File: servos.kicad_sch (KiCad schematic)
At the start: 14 parts, among them J10 Conn_01x03, J11 Conn_01x03, J6 Conn_01x03, J7 Conn_01x03, J8 Conn_01x03, J9 Conn_01x03, U10 INA745A, U11 INA745A, U12 INA745A, U13 INA745A, U15 SN74LVC8T245, U6 INA745A, U9 INA745A

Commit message: got it to fit in about the right shape
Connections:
- net +3V3: now also U15.1 (V_{CCA})
- net GND: now also U15.11 (GND), U15.12 (GND), U15.13 (GND)
- net +5V: now reaches U15.23 (V_{CCB}), U15.24 (V_{CCB})
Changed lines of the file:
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@@
+	)
+	(symbol
+		(lib_id "power:+3V3")
+		(at 341.63 46.99 0)
+		(unit 1)
+		(exclude_from_sim no)
+		(in_bom yes)
+		(on_board yes)
+		(dnp no)
+		(fields_autoplaced yes)
+		(property "Reference" "#PWR081"
+			(at 341.63 50.8 0)
+			(effects
+				(font
+					(size 1.27 1.27)
+				)
+				(hide yes)
+			)
+		)
+		(property "Value" "+3V3"
+			(at 341.63 41.91 0)
+			(effects
+				(font
+					(size 1.27 1.27)
+				)
+			)
+		)
+		(property "Footprint" ""
+			(at 341.63 46.99 0)
+			(effects
+				(font
+					(size 1.27 1.27)
+				)
+				(hide yes)
+			)
+		)
+		(property "Datasheet" ""
+			(at 341.63 46.99 0)
+			(effects
+				(font
+					(size 1.27 1.27)
+				)
+				(hide yes)
+			)
+		)
+		(property "Description" "Power symbol creates a global label with name \"+3V3\""
+			(at 341.63 46.99 0)
+			(effects
+				(font
+					(size 1.27 1.27)
+				)
+				(hide yes)
+			)
+		)
+		(pin "1"
+		)
+		(instances
+			(project ""
+				(path "/49232f62-a438-4b3e-9be5-c2b3074d8de1/d4349b58-c0d1-4d8c-92d6-ed5d2b18f2a0"
+					(reference "#PWR081")
+					(unit 1)
+				)
+			)
+		)
 	)
 	(symbol
@@
 	)
 	(symbol
+		(lib_id "power:GND")
+		(at 344.17 102.87 0)
+		(unit 1)
+		(exclude_from_sim no)
+		(in_bom yes)
+		(on_board yes)
+		(dnp no)
+		(fields_autoplaced yes)
+		(property "Reference" "#PWR083"
+			(at 344.17 109.22 0)
+			(effects
+				(font
+					(size 1.27 1.27)
+				)
+				(hide yes)
+			)
+		)
+		(property "Value" "GND"
+			(at 344.17 107.95 0)
+			(effects
+				(font
+					(size 1.27 1.27)
+				)
+			)
+		)
+		(property "Footprint" ""
+			(at 344.17 102.87 0)
+			(effects
+				(font
+					(size 1.27 1.27)
+				)
+				(hide yes)
+			)
+		)
+		(property "Datasheet" ""
+			(at 344.17 102.87 0)
+			(effects
+				(font
+					(size 1.27 1.27)
+				)
+				(hide yes)
+			)
+		)
+		(property "Description" "Power symbol creates a global label with name \"GND\" , ground"
+			(at 344.17 102.87 0)
+			(effects
+				(font
+					(size 1.27 1.27)
+				)
+				(hide yes)
+			)
+		)
+		(pin "1"
+		)
+		(instances
+			(project ""
+				(path "/49232f62-a438-4b3e-9be5-c2b3074d8de1/d4349b58-c0d1-4d8c-92d6-ed5d2b18f2a0"
+					(reference "#PWR083")
+					(unit 1)
+				)
+			)
+		)
+	)
+	(symbol
 		(lib_id "power:GND1")
 		(at 243.84 73.66 0)
@@
 					(unit 1)
 				)
+			)
+		)
+	)
+	(symbol
+		(lib_id "power:+5V")
+		(at 346.71 46.99 0)
+		(unit 1)
+		(exclude_from_sim no)
+		(in_bom yes)
+		(on_board yes)
+		(dnp no)
+		(fields_autoplaced yes)
+		(property "Reference" "#PWR082"
+			(at 346.71 50.8 0)
+			(effects
+				(font
+					(size 1.27 1.27)
+				)
+				(hide yes)
+			)
+		)
+		(property "Value" "+5V"
+			(at 346.71 41.91 0)
+			(effects
+				(font
+					(size 1.27 1.27)
+				)
+			)
+		)
+		(property "Footprint" ""
+			(at 346.71 46.99 0)
+			(effects
+				(font
+					(size 1.27 1.27)
+				)
+				(hide yes)
+			)
+		)
+		(property "Datasheet" ""
+			(at 346.71 46.99 0)
+			(effects
+				(font
+					(size 1.27 1.27)
+				)
+				(hide yes)
+			)
+		)
+		(property "Description" "Power symbol creates a global label with name \"+5V\""
+			(at 346.71 46.99 0)
+			(effects
+				(font
+					(size 1.27 1.27)
+				)
+				(hide yes)
+			)
+		)
+		(pin "1"
+		)
+		(instances
+			(project ""
+				(path "/49232f62-a438-4b3e-9be5-c2b3074d8de1/d4349b58-c0d1-4d8c-92d6-ed5d2b18f2a0"
+					(reference "#PWR082")
+					(unit 1)
+				)

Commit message: add 3d models and do other stuff
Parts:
- removed U15: SN74LVC8T245, Package_SO:TSSOP-24_4.4x7.8mm_P0.65mm, symbol Logic_LevelTranslator:SN74LVC8T245
- added C19, C20, C21, C22, C23, C24: 100n, Capacitor_SMD:C_0402_1005Metric, symbol Device:C_Small
- J10, J11, J6, J7, J8, J9: footprint Connector_JST:JST_VH_B3P-VH-B_1x03_P3.96mm_Vertical -> beavs-footprints:JST_VH_B3P-VH-B_1x03_P3.96mm_Vertical_model
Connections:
- net +3V3: now also C19.1, C20.1, C21.1, C22.1, C23.1, C24.1
- net GND: now also C19.2, C20.2, C21.2, C22.2, C23.2, C24.2
- net S4: now reaches J9.1 (Pin_1)
- net S1: now reaches J6.1 (Pin_1)
- net S6: now reaches J11.1 (Pin_1)
- net S5: now reaches J10.1 (Pin_1)
- net S2: now reaches J7.1 (Pin_1)
- net S3: now reaches J8.1 (Pin_1)

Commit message: add some TVS diodes
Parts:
- added NT2, NT3, NT4, NT5, NT6: NetTie_2, NetTie:NetTie-2_SMD_Pad2.0mm, symbol Device:NetTie_2
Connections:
- net GND: now also NT2.2, NT3.2, NT4.2, NT5.2, NT6.2
- net GND1: now also NT2.1, NT3.1, NT4.1, NT5.1, NT6.1

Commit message: update schematics and add 3d models
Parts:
- C19, C20, C21, C22, C23, C24: LCSC (none) -> C1525
- U10, U11, U12, U13, U6, U9: LCSC (none) -> C35213810
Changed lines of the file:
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@@
 			)
 		)
+		(property "LCSC" ""
+			(at 80.01 176.53 0)
+			(effects
+				(font
+					(size 1.27 1.27)
+				)
+				(hide yes)
+			)
+		)
 		(pin "2"
 		)
@@
 			)
 		)
+		(property "LCSC" "C35213810"
+			(at 59.69 128.27 0)
+			(effects
+				(font
+					(size 1.27 1.27)
+				)
+				(hide yes)
+			)
+		)
 		(pin "1"
 		)
@@
 			)
 		)
+		(property "LCSC" ""
+			(at 93.98 116.84 0)
+			(effects
+				(font
+					(size 1.27 1.27)
+				)
+				(hide yes)
+			)
+		)
 		(pin "2"
 		)
@@
 			)
 		)
+		(property "LCSC" "C1525"
+			(at 53.34 43.18 0)
+			(effects
+				(font
+					(size 1.27 1.27)
+				)
+				(hide yes)
+			)
+		)
 		(pin "1"
 		)
@@
 			)
 		)
+		(property "LCSC" ""
+			(at 80.01 177.8 0)
+			(effects
+				(font
+					(size 1.27 1.27)
+				)
+				(hide yes)
+			)
+		)
 		(pin "2"
 		)
@@
 			)
 		)
+		(property "LCSC" ""
+			(at 93.98 57.15 0)
+			(effects
+				(font
+					(size 1.27 1.27)
+				)
+				(hide yes)
+			)
+		)
 		(pin "2"
 		)
@@
 			)
 		)
+		(property "LCSC" "C1525"
+			(at 212.09 104.14 0)
+			(effects
+				(font
+					(size 1.27 1.27)
+				)
+				(hide yes)
+			)
+		)
 		(pin "1"
 		)
@@
 			)
 		)
+		(property "LCSC" "C35213810"
+			(at 138.43 68.58 0)
+			(effects
+				(font
+					(size 1.27 1.27)
+				)
+				(hide yes)
+			)
+		)
 		(pin "1"
 		)
@@
 			)
 		)
+		(property "LCSC" "C1525"
+			(at 133.35 102.87 0)
+			(effects
+				(font
+					(size 1.27 1.27)
+				)
+				(hide yes)
+			)
+		)
 		(pin "1"
 		)
@@
 			)
 		)
+		(property "LCSC" "C35213810"
+			(at 218.44 129.54 0)
+			(effects
+				(font
+					(size 1.27 1.27)
+				)
+				(hide yes)
+			)
+		)
 		(pin "1"
 		)
@@
 			)
 		)
+		(property "LCSC" ""
+			(at 252.73 118.11 0)
+			(effects
+				(font
+					(size 1.27 1.27)
+				)
+				(hide yes)
+			)
+		)
 		(pin "2"
 		)
@@
 			)
 		)
+		(property "LCSC" ""
+			(at 173.99 116.84 0)
+			(effects
+				(font
+					(size 1.27 1.27)
+				)
+				(hide yes)
+			)
+		)
 		(pin "2"
 		)
@@
 			)
 		)
+		(property "LCSC" "C1525"
+			(at 212.09 43.18 0)
+			(effects
+				(font
+					(size 1.27 1.27)
+				)
+				(hide yes)
+			)
+		)
 		(pin "1"
 		)
@@
 			)
 		)
+		(property "LCSC" "C35213810"
+			(at 218.44 68.58 0)
+			(effects
+				(font
+					(size 1.27 1.27)
+				)
+				(hide yes)
+			)
+		)
 		(pin "1"
 		)
@@
 			)
 		)
+		(property "LCSC" ""
+			(at 80.01 181.61 0)
+			(effects
+				(font
+					(size 1.27 1.27)
+				)
+				(hide yes)
+			)
+		)
 		(pin "2"
 		)
@@
 			)
 		)
+		(property "LCSC" "C35213810"
+			(at 59.69 68.58 0)
+			(effects
+				(font
+					(size 1.27 1.27)
+				)
+				(hide yes)
+			)
+		)
 		(pin "1"
 		)
@@
 			)
 		)
+		(property "LCSC" "C1525"
+			(at 53.34 104.14 0)
+			(effects
+				(font
+					(size 1.27 1.27)
+				)
+				(hide yes)
+			)
+		)
 		(pin "1"
 		)
@@
 			)
 		)
+		(property "LCSC" ""
+			(at 172.72 57.15 0)
+			(effects
+				(font
+					(size 1.27 1.27)
+				)
+				(hide yes)
+			)
+		)
 		(pin "2"
 		)
@@
 			)
 		)
+		(property "LCSC" "C35213810"
+			(at 139.7 128.27 0)
+			(effects
+				(font
+					(size 1.27 1.27)
+				)
+				(hide yes)
+			)
+		)
 		(pin "1"
 		)
@@
 			)
 		)
+		(property "LCSC" ""
+			(at 80.01 182.88 0)
+			(effects
+				(font
+					(size 1.27 1.27)
+				)
+				(hide yes)
+			)
+		)
 		(pin "2"
 		)
@@
 			)
 		)
+		(property "LCSC" ""
+			(at 252.73 57.15 0)
+			(effects
+				(font
+					(size 1.27 1.27)
+				)
+				(hide yes)
+			)
+		)
 		(pin "2"
 		)
@@
 			)
 		)
+		(property "LCSC" ""
+			(at 80.01 179.07 0)
+			(effects
+				(font
+					(size 1.27 1.27)
+				)
+				(hide yes)
+			)
+		)
 		(pin "2"
 		)
@@
 			)
 		)
+		(property "LCSC" ""
+			(at 80.01 180.34 0)
+			(effects
+				(font
+					(size 1.27 1.27)
+				)
+				(hide yes)
+			)
+		)
 		(pin "2"
 		)
@@
 			(at 132.08 43.18 0)
 			(effects
+				(font
+					(size 1.27 1.27)
+				)
+				(hide yes)
+			)
+		)
+		(property "LCSC" "C1525"
+			(at 132.08 43.18 0)
+			(effects

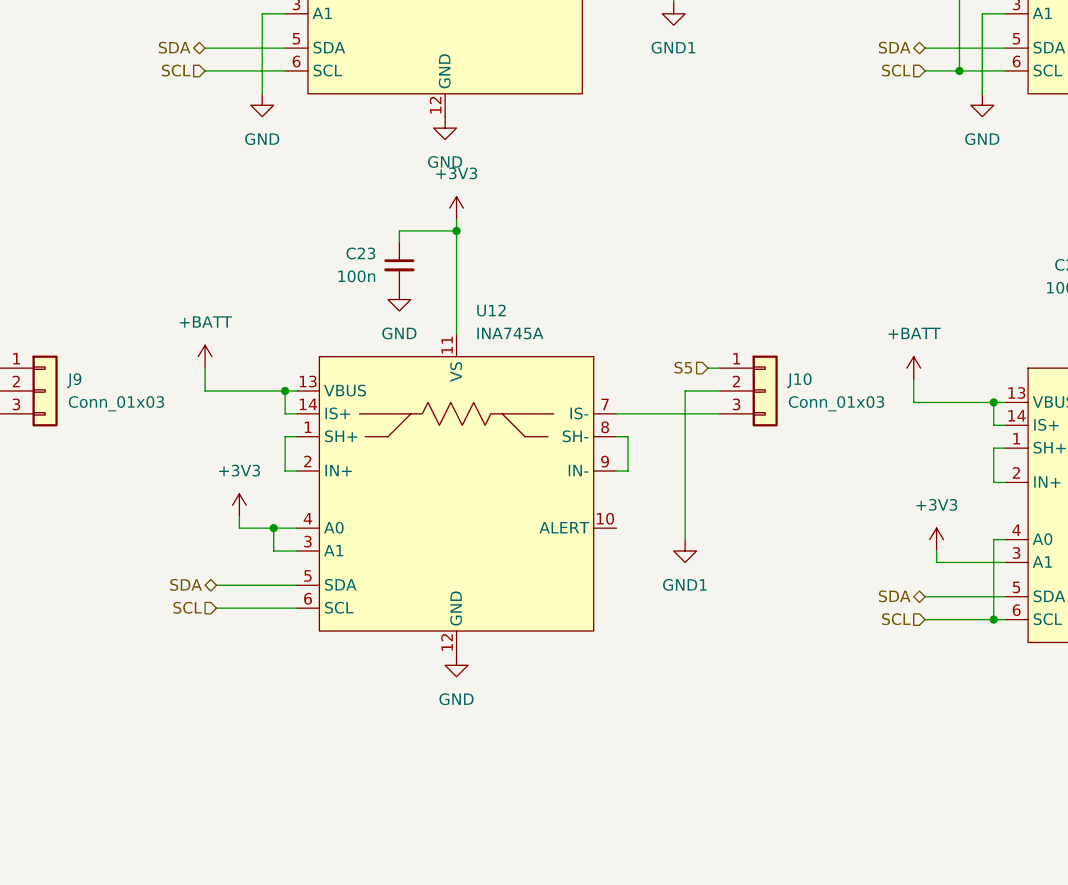
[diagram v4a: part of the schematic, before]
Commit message: stapling vias, silk, minor schematic tweaks
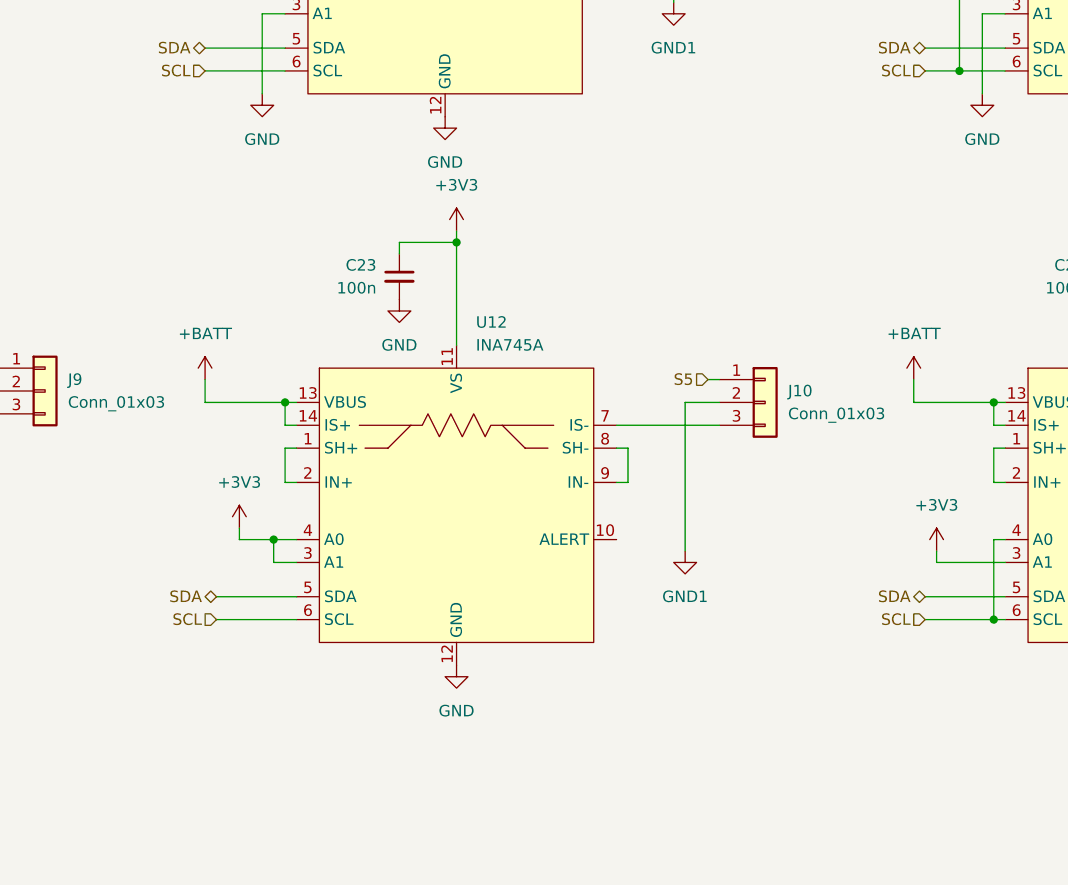
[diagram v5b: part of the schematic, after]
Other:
- moved on the sheet: C23, J10, U12

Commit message: capacitor spam, needs current limiting
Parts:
- added C27, C30, C31, C32, C33, C34, C35, C36, C37, C38, C39, C40, C41, C42, C43, C44: 47u, Capacitor_SMD:C_1206_3216Metric, symbol Device:C_Small
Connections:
- net +BATT: now also C35.1, C36.1, C37.1, C38.1, C39.1, C40.1, C41.1, C42.1, C43.1, C44.1
- net GND1: now also C27.2, C30.2, C31.2, C32.2, C33.2, C34.2, C35.2, C36.2, C37.2, C38.2, C39.2, C40.2, C41.2, C42.2, C43.2, C44.2
- net at J9.3 (Pin_3), U11.7 (IS-): now also C34.1
- net at J6.3 (Pin_3), U6.7 (IS-): now also C27.1
- net at J7.3 (Pin_3), U9.7 (IS-): now also C30.1
- net at J11.3 (Pin_3), U13.7 (IS-): now also C32.1
- net at J10.3 (Pin_3), U12.7 (IS-): now also C33.1
- net at J8.3 (Pin_3), U10.7 (IS-): now also C31.1

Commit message: finished power, checked most sensor schematics
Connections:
- net GND: now also U10.10 (ALERT), U11.10 (ALERT), U12.10 (ALERT), U13.10 (ALERT), U6.10 (ALERT), U9.10 (ALERT)

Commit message: bigger pours for FETs, various cleanup, switching to different level shifter
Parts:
- C27, C30, C31, C32, C33, C34, C35, C36, C37, C38, C39, C40, C41, C42, C43, C44: digikey (none) -> 490-5528-1-ND
- J10, J11, J6, J7, J8, J9: digikey (none) -> 455-B3P-VH-ND
